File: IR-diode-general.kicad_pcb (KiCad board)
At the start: 2 copper layers, 80 x 20.5 mm, 27 parts, among them J1 PJ-102A, J2 USB4105-GF-A, J3 SM06B-SRSS-TB-LF-SN, J4 SM06B-SRSS-TB-LF-SN, U1 MP2483DQ-LF-P, U2 AZ1117CH-5.0TRG1

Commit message: Layout and schematic updates
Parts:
- added C10: C_22u_0603, antmicro-footprints:C_0603_1608Metric, F.Cu at (163.8, 83.3)
- added C11: C_22u_0603, antmicro-footprints:C_0603_1608Metric, F.Cu at (162.1, 86.7)
- added L2: TFM252012ALMA3R3MTAA, antmicro-footprints:L_1008_2520Metric, F.Cu at (168.9, 76.5)
- added POT1: R0141-2-20k, antmicro-footprints:R0141-2-20k, F.Cu at (99.0, 45.0)
- added R8: R_6k8_0402, antmicro-footprints:0402-res, F.Cu at (166.4, 88.8)
- added R9: R_1k3_0402, antmicro-footprints:R_0402_1005Metric, F.Cu at (168.7, 80.7)
- C6: value C_10u_0805 -> C_10p_0402; footprint antmicro-footprints:0805-cap -> antmicro-footprints:C_0402_1005Metric
- C7: value C_22u_0402 -> C_100n_0402
- J1: value PJ-102A -> BarrelJack_3167288; footprint antmicro-footprints:Barrel_Jack_5.5mmODx2.1mmID_PJ-102A -> antmicro-footprints:BarrelJack_3167288_Horizontal
- R2: value R_100k_0402 -> R_39k_0402; footprint antmicro-footprints:R_0402_1005Metric -> antmicro-footprints:0402-res
- U2: value AZ1117CH-5.0TRG1 -> AP62301Z6-7; footprint antmicro-footprints:SOT-223 -> antmicro-footprints:SOT-563
- moved U2 69.8 mm to (163.5, 80.3)
- moved C7 64.9 mm to (158.7, 83.3)
- moved J1 64.6 mm to (154.9, 56.6), turned to 90 degrees
- moved C6 61.3 mm to (159.8, 79.9), turned to 0 degrees
- moved POT1 33.8 mm to (115.2, 75.3)
- moved C9 16.6 mm to (89.3, 50.0)
- moved R2 14.9 mm to (153.1, 42.9), turned to 180 degrees
- moved J2 13.9 mm to (88.2, 55.9), turned to -90 degrees
- moved C4 13.7 mm to (149.2, 43.0), turned to 180 degrees
- moved R4 13.3 mm to (145.6, 44.9), turned to 90 degrees
- moved R1 13.2 mm to (146.2, 55.0), turned to -90 degrees
- moved C5 12.8 mm to (153.1, 44.1), turned to 180 degrees
- moved R3 11.8 mm to (146.8, 44.9), turned to -90 degrees
- moved R7 10.8 mm to (148.5, 55.0), turned to -90 degrees
- moved C3 9.08 mm to (152.8, 46.1), turned to 90 degrees
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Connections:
- C6 pad 1: GND -> +12V
- C6 pad 2: +12V -> GND
- C7 pad 1: GND -> Net-(U2-Pad4)
- C7 pad 2: Net-(C7-Pad2) -> Net-(U2-Pad2)
- D2 pad 2: C_in -> C_out
- D2 pad 3: C_in -> C_out
- J2 pad A4: Net-(C7-Pad2) -> Net-(J2-PadA4)
- J2 pad A9: Net-(C7-Pad2) -> Net-(J2-PadA4)
- J2 pad B4: Net-(C7-Pad2) -> Net-(J2-PadA4)
- J2 pad B9: Net-(C7-Pad2) -> Net-(J2-PadA4)
- J3 pad 1: C_in -> unconnected-(J3-Pad1)
- J3 pad 2: C_out -> unconnected-(J3-Pad2)
- J3 pad 3: A_in -> unconnected-(J3-Pad3)
- J3 pad 4: +12V -> unconnected-(J3-Pad4)
- J3 pad 5: GND -> unconnected-(J3-Pad5)
- J3 pad S1: GND -> Net-(J3-PadS1)
- J3 pad S2: GND -> Net-(J3-PadS1)
- J4 pad 1: C_in -> unconnected-(J4-Pad1)
- J4 pad 2: C_out -> unconnected-(J4-Pad2)
- J4 pad 3: A_in -> unconnected-(J4-Pad3)
- R5 pad 1: Net-(POT1-Pad3) -> Net-(R5-Pad1)
- R7 pad 2: C_in -> C_out
- U1 pad 7: Net-(POT1-Pad2) -> Net-(U1-Pad7)
- U2 pad 1: GND -> +12V
- U2 pad 2: Net-(C7-Pad2) -> Net-(U2-Pad2)
- U2 pad 3: +12V -> GND
- U2 pad 4: Net-(C7-Pad2) -> Net-(U2-Pad4)
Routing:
- net Net-(POT1-Pad2): track 66.2 -> 0.00 mm
- net C_out: track 47.5 -> 0.00 mm, vias 2 -> 0
- net Net-(D2-Pad1): track 31.1 -> 0.00 mm
- net +12V: track 28.5 -> 0.00 mm
- net GND: track 27.1 -> 0.00 mm
- net C_in: track 26.0 -> 0.00 mm
- net Net-(C7-Pad2): track 18.7 -> 0.00 mm
- net A_in: track 12.4 -> 0.00 mm
- net Net-(C3-Pad1): track 7.14 -> 0.00 mm
- net Net-(C8-Pad2): track 6.69 -> 0.00 mm
- net Net-(POT1-Pad3): track 4.00 -> 0.00 mm
- net Net-(R3-Pad2): track 3.07 -> 0.00 mm
- net Net-(C5-Pad2): track 2.49 -> 0.00 mm
- net Net-(C4-Pad2): track 1.57 -> 0.00 mm
- net Net-(C3-Pad2): track 1.53 -> 0.00 mm
- removed copper zone on B.Cu, net GND
- removed copper zone on F.Cu, net GND

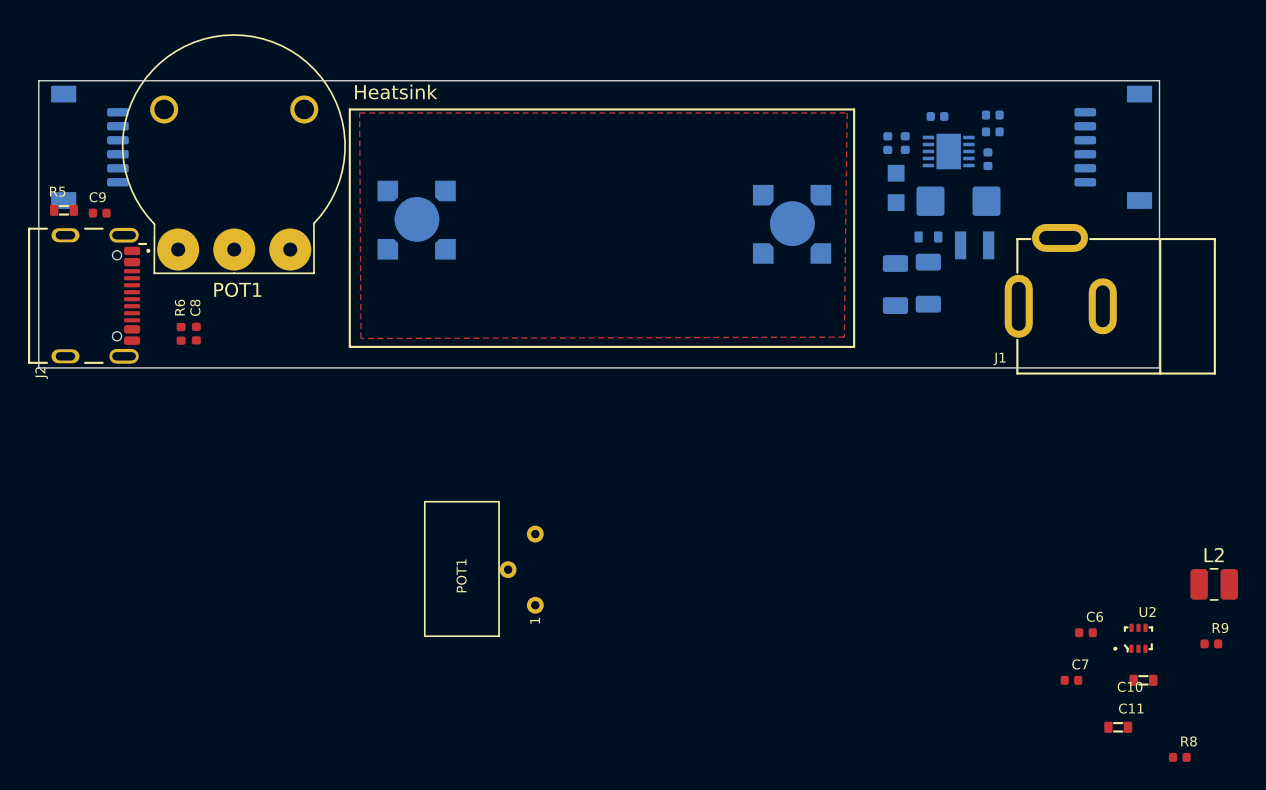
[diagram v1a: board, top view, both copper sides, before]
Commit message: Layout tweaks
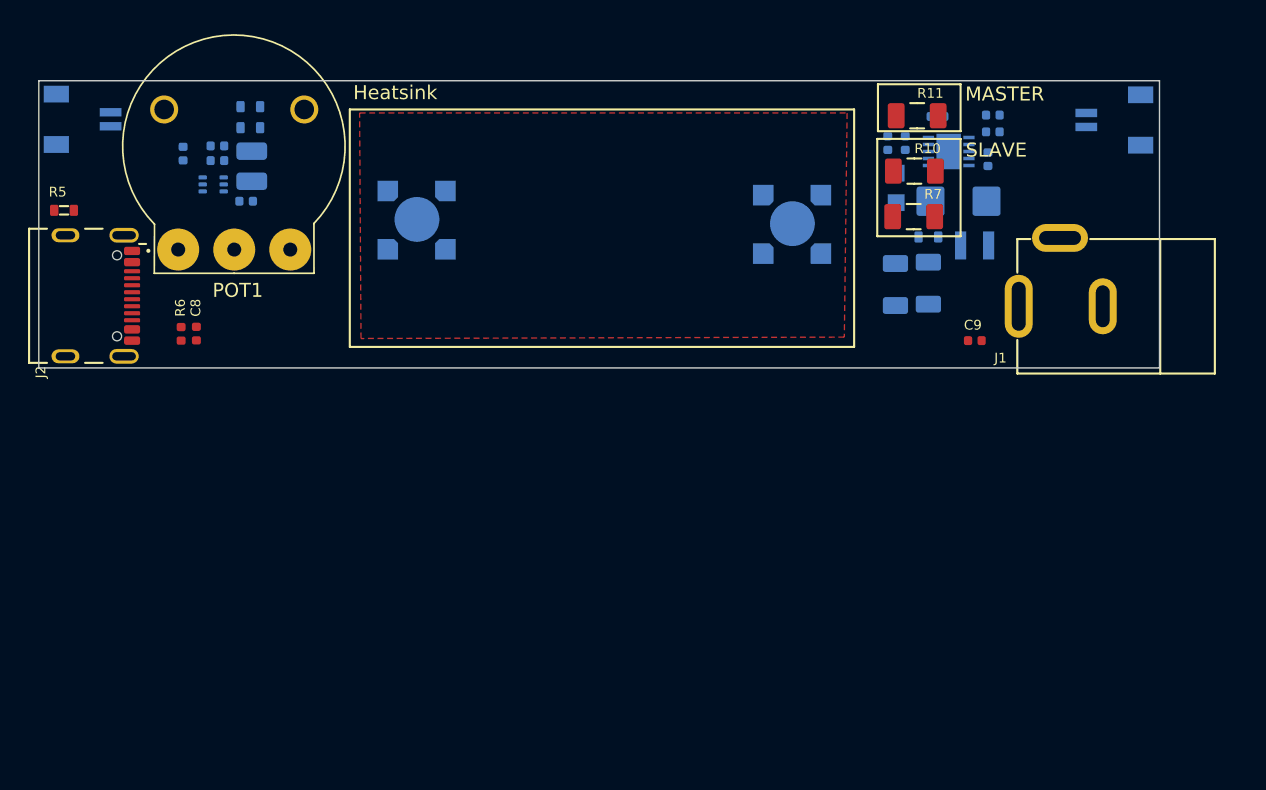
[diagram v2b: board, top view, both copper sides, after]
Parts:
- removed J3, J4: SM06B-SRSS-TB-LF-SN, antmicro-footprints:JST_SM06B-SRSS-TB-LF-SN
- removed the POT1 at (115.2, 75.3)
- added R10: R_0R_1206, antmicro-footprints:R_1206_3216Metric, F.Cu at (147.5, 47.0)
- added R11: R_0R_1206, antmicro-footprints:R_1206_3216Metric, F.Cu at (147.7, 43.0)
- added R7: R_0R_1206, antmicro-footprints:R_1206_3216Metric, F.Cu at (147.4, 50.2)
- added U3: SM02B-SRSS-TB-LF-SN, antmicro-footprints:JST_SM02B-SRSS-TB(LF)(SN), B.Cu at (161.8, 43.3)
- added U4: SM02B-SRSS-TB-LF-SN, antmicro-footprints:JST_SM02B-SRSS-TB(LF)(SN), B.Cu at (88.2, 43.2)
- C10, C11, C6, C7, L2, R8, R9, U2: moved to B.Cu
- U1: value MP2483DQ-LF-P -> QFN10_MP2483DQ_MNP
- moved R8 81.4 mm to (97.8, 45.1)
- moved R9 81.3 mm to (95.3, 45.7), turned to 90 degrees
- moved C11 76.2 mm to (100.1, 42.4), turned to 180 degrees
- moved C10 75.0 mm to (100.1, 43.9)
- moved L2 74.9 mm to (100.2, 46.6), turned to 90 degrees
- moved U2 73.6 mm to (97.5, 47.9), turned to -90 degrees
- moved C6 70.6 mm to (97.8, 46.2), turned to 180 degrees
- moved C7 68.1 mm to (99.8, 49.1), turned to 180 degrees
- moved C9 63.1 mm to (151.8, 59.0)
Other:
- board text added: "MASTER"
- board text added: "SLAVE"

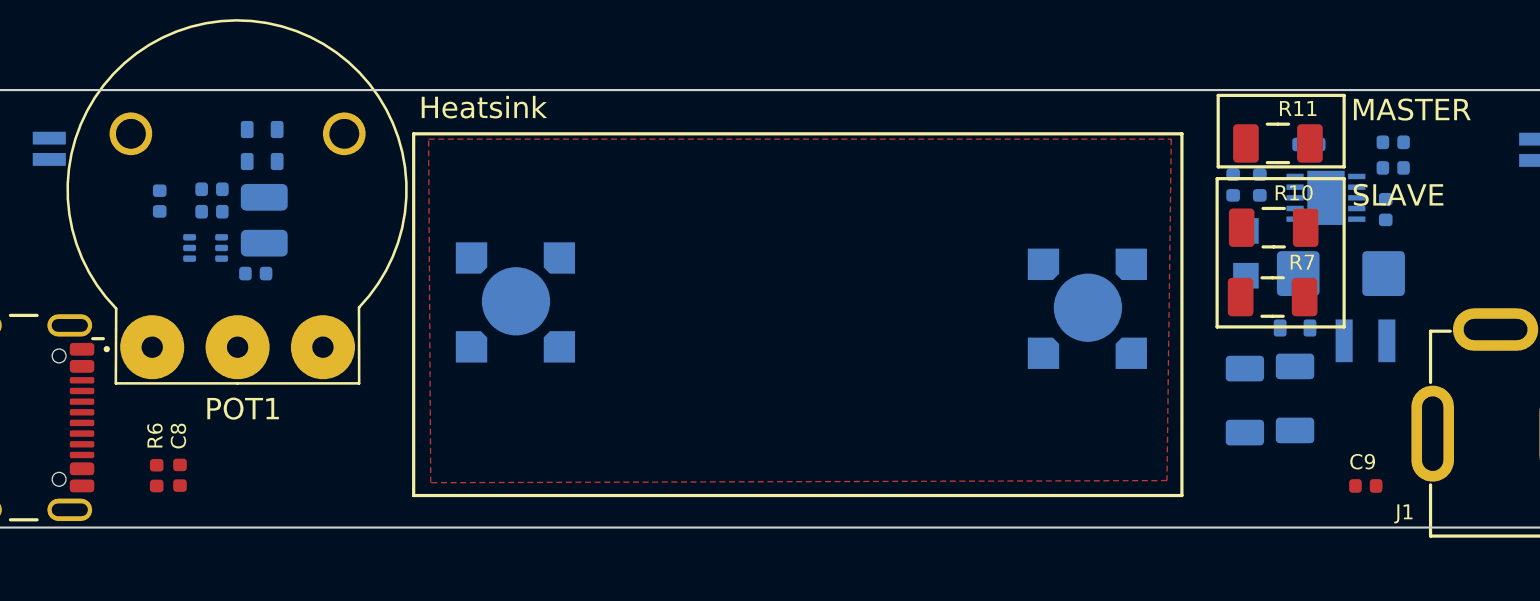
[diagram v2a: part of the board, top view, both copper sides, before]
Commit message: Added pull down resistors on USB
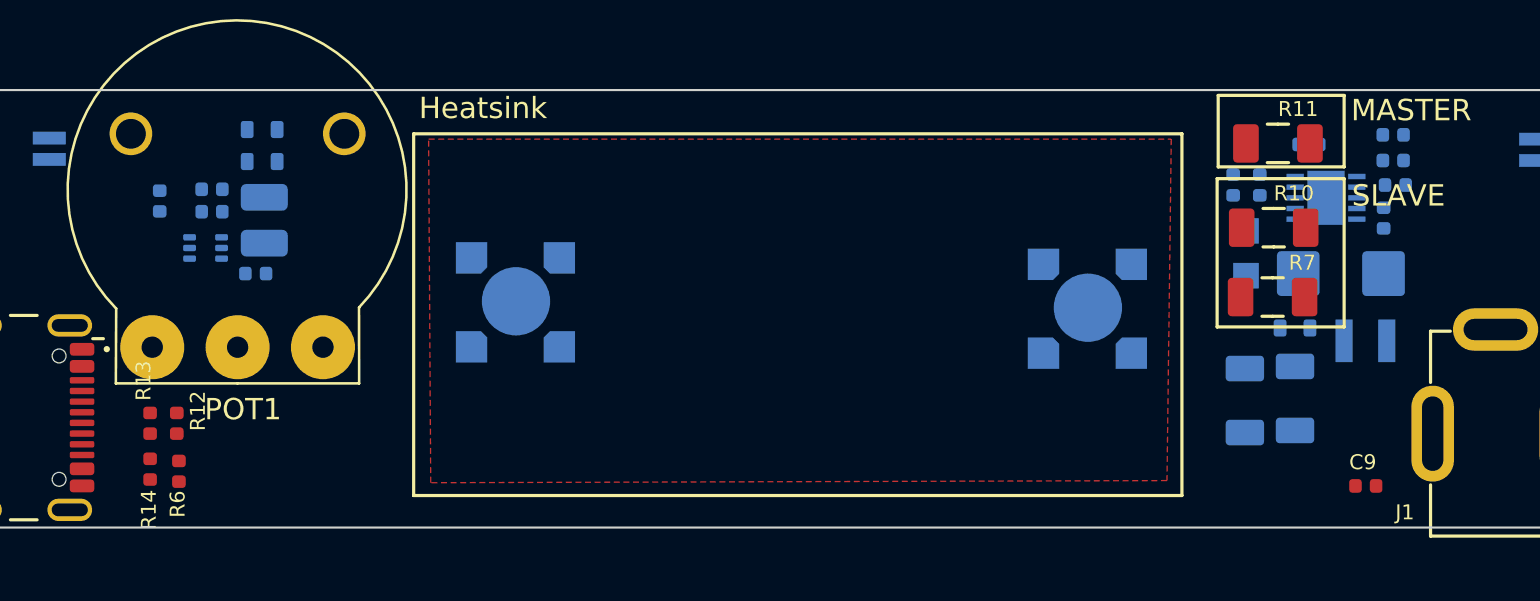
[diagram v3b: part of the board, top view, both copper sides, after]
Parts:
- added R12: R_10k_0402, antmicro-footprints:R_0402_1005Metric, F.Cu at (96.1, 56.1)
- added R13: R_100R_0402, antmicro-footprints:R_0402_1005Metric, F.Cu at (94.8, 56.1)
- added R14: R_10k_0402, antmicro-footprints:R_0402_1005Metric, F.Cu at (94.8, 58.3)
- C8: moved to B.Cu
- POT1: footprint antmicro-footprints:R0141-2-20k -> antmicro-footprints:Potentiometer_SRPassives_R0141-2_Horizontal
- moved C8 58.6 mm to (153.2, 45.0), turned to 180 degrees
- moved R6 1.06 mm to (96.2, 58.4)
- moved C3 0.41 mm to (152.7, 46.5)
- moved C5 0.35 mm to (153.1, 43.8)
- moved R2 0.35 mm to (153.1, 42.6)
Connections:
- C2 pad 2: A_in -> Net-(C2-Pad2)
- C8 pad 2: Net-(C8-Pad2) -> Net-(POT1-Pad3)
- D1 pad 1: GND -> (no net)
- D1 pad 2: Net-(C3-Pad1) -> (no net)
- D2 pad 2: C_out -> A_in
- D2 pad 3: C_out -> A_in
- D3 pad 1: C_out -> FB
- D3 pad 4: C_out -> FB
- J2 pad A6: unconnected-(J2-PadA6) -> Net-(J2-PadA6)
- J2 pad A7: unconnected-(J2-PadA7) -> Net-(J2-PadA7)
- J2 pad B6: unconnected-(J2-PadB6) -> Net-(J2-PadA6)
- J2 pad B7: unconnected-(J2-PadB7) -> Net-(J2-PadA7)
- L1 pad 2: A_in -> Net-(C2-Pad2)
- R1 pad 2: C_out -> FB
- R3 pad 1: A_in -> Net-(C2-Pad2)
- R6 pad 2: Net-(C8-Pad2) -> Net-(POT1-Pad1)
- R7 pad 1: A_in -> Net-(C2-Pad2)
- U1 pad 4: C_out -> FB
- U1 pad 7: Net-(U1-Pad7) -> Net-(POT1-Pad3)
- U2 pad 5: unconnected-(U2-Pad5) -> Net-(U2-Pad5)

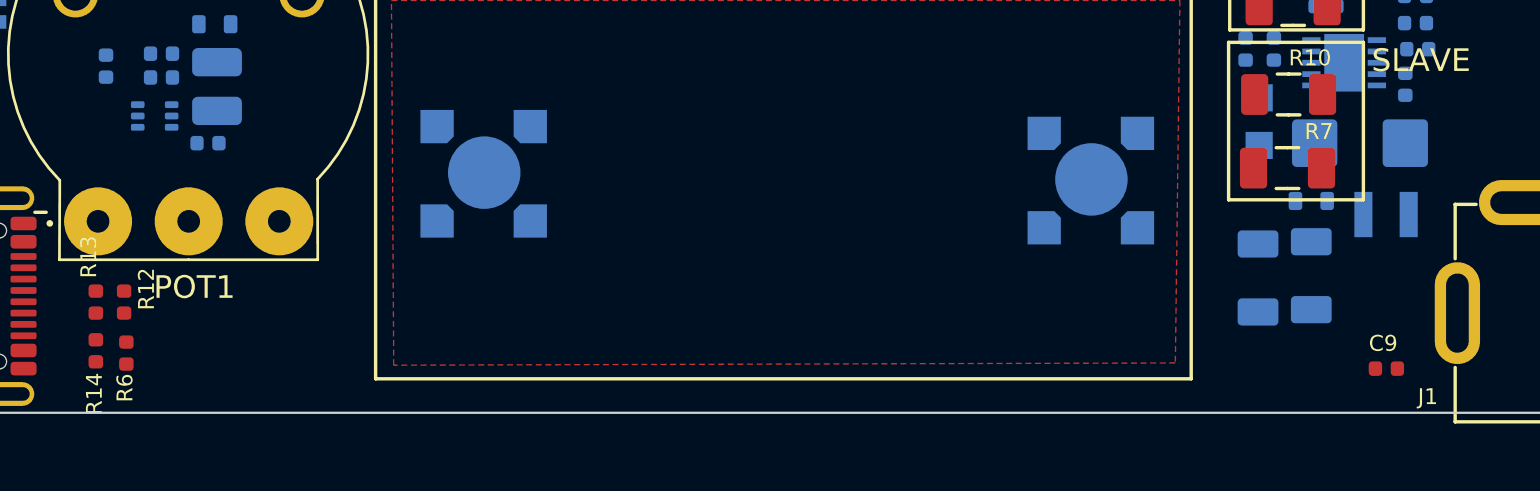
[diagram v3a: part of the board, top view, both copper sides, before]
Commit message: B2B connectors symbol adjusted
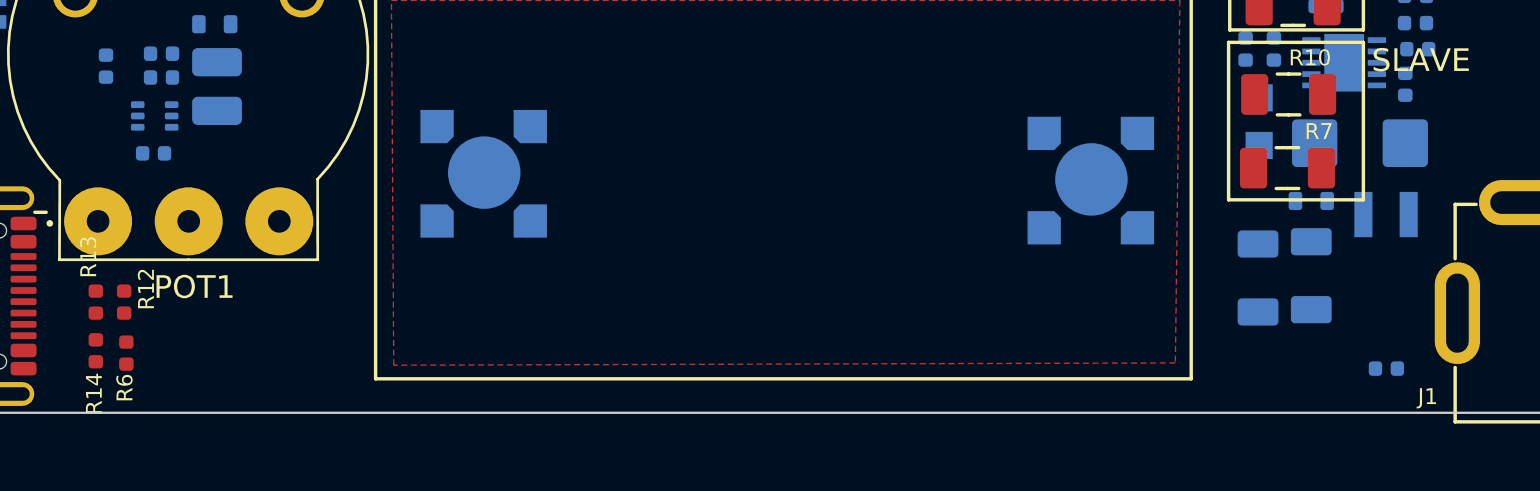
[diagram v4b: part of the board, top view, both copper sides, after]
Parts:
- C9: moved to B.Cu
- moved C7 2.44 mm to (97.4, 49.5), turned to 0 degrees
- turned C9 to 0 degrees

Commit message: Finalized board layout
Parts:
- removed the R7 at (147.4, 50.2)
- added C12: C_100n_0402, antmicro-footprints:C_0402_1005Metric, F.Cu at (93.2, 58.7)
- added C13: C_100n_0402, antmicro-footprints:C_0402_1005Metric, F.Cu at (93.2, 53.1)
- R10, R11, R5: moved to B.Cu
- moved D3 26.8 mm to (138.7, 50.8), turned to 180 degrees
- moved D2 26.8 mm to (111.9, 50.8), turned to 180 degrees
- moved R5 15.8 mm to (102.5, 48.4), turned to 90 degrees
- moved R11 14.7 mm to (161.3, 48.7), turned to 180 degrees
- moved R10 9.99 mm to (156.9, 43.7), turned to 90 degrees
- moved R9 2.24 mm to (94.9, 47.9)
- moved R1 1.97 mm to (144.6, 53.9), turned to 180 degrees
- moved J1 1.25 mm to (153.7, 56.6)
- moved POT1 0.56 mm to (99.5, 44.9)
- moved C9 0.35 mm to (151.5, 59.2)
- moved C4 0.11 mm to (149.1, 43.1)
- moved R6 0.10 mm to (96.1, 58.4)
- turned C1 to -90 degrees
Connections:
- net Net-(C10-Pad2) renamed /LED DRIVER & USB-C Power output/VBUS
- C2 pad 2: Net-(C2-Pad2) -> SW
- C8 pad 2: Net-(POT1-Pad3) -> Net-(C8-Pad2)
- D2 pad 5: unconnected-(D2-Pad5) -> Thermal
- D3 pad 5: unconnected-(D3-Pad5) -> Thermal
- L1 pad 2: Net-(C2-Pad2) -> SW
- POT1 pad 1: (no net) -> Net-(POT1-Pad1)
- POT1 pad 2: (no net) -> Net-(POT1-Pad2)
- POT1 pad 3: (no net) -> Net-(C8-Pad2)
- R11 pad 2: Net-(C2-Pad2) -> SW
- R3 pad 1: Net-(C2-Pad2) -> SW
- R7 pad 1: Net-(C2-Pad2) -> A_in
- R7 pad 2: C_out -> SW
- U1 pad 7: Net-(POT1-Pad3) -> Net-(C8-Pad2)
- U3 pad 2: A_in -> C_out
- U3 pad 3: (no net) -> GND
- U3 pad 4: (no net) -> GND
- U4 pad 1: C_out -> A_in
- U4 pad 3: (no net) -> GND
- U4 pad 4: (no net) -> GND
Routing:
- net A_in: track 0.00 -> 89.6 mm, vias 0 -> 2
- net Net-(C8-Pad2): track 0.00 -> 65.4 mm
- net FB: track 0.00 -> 38.7 mm, vias 0 -> 1
- net Net-(D2-Pad1): track 0.00 -> 36.9 mm
- net GND: track 0.00 -> 33.0 mm, vias 0 -> 3
- net +12V: track 0.00 -> 32.0 mm, vias 0 -> 2
- net /LED DRIVER & USB-C Power output/VBUS: track 0.00 -> 31.2 mm, vias 0 -> 1
- net SW: track 0.00 -> 28.3 mm, vias 0 -> 3
- net C_out: track 0.00 -> 11.3 mm, vias 0 -> 1
- net Net-(C3-Pad1): track 0.00 -> 7.86 mm
- net Net-(POT1-Pad1): track 0.00 -> 7.82 mm
- net Net-(J2-PadA6): track 0.00 -> 6.96 mm
- net Net-(J2-PadA7): track 0.00 -> 6.22 mm
- net Net-(R8-Pad1): track 0.00 -> 6.08 mm
- net Net-(POT1-Pad2): track 0.00 -> 4.54 mm
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- added copper zone on F.Cu, net +12V
- added copper zone on B.Cu, net GND
- added copper zone on F.Cu, net GND
- added copper zone on B.Cu, net Thermal
- added copper zone on F.Cu, net Thermal
- removed copper zone on F.Cu, net (none)
